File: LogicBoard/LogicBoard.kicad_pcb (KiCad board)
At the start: 2 copper layers, 96.5 x 43.9 mm, 19 parts, among them J1 Conn_01x50, J2 Conn_01x10, J3 Conn_interconn, J4 Conn_02x5_CODEC, U1 STM32H757XIHx

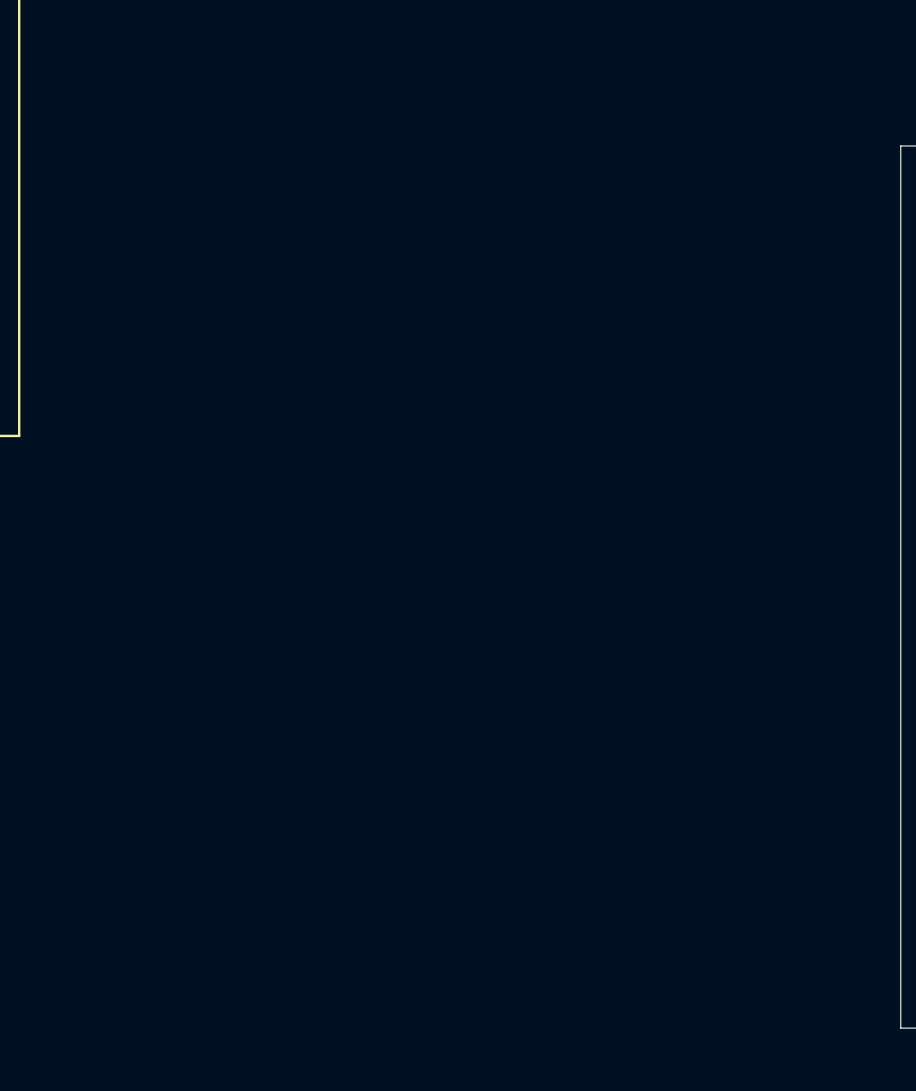
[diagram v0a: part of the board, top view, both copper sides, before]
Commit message: added jlcpcb nums to some parts
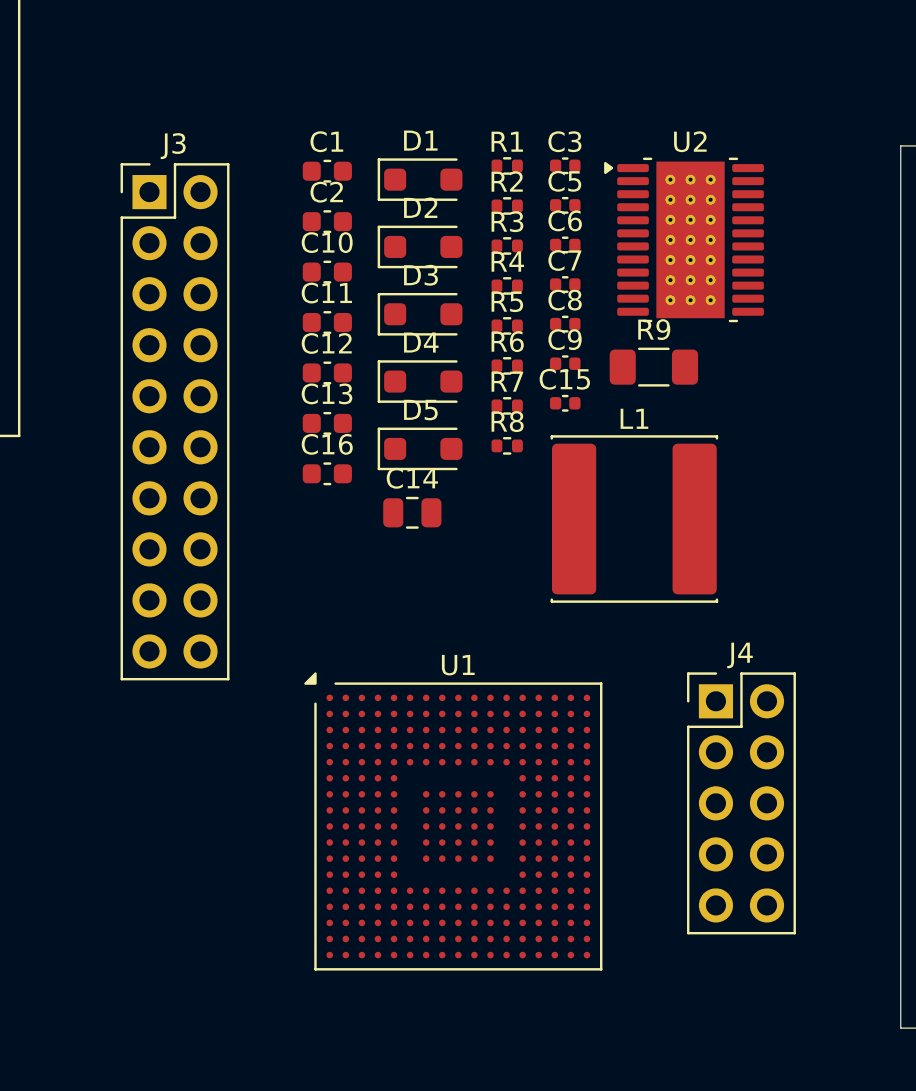
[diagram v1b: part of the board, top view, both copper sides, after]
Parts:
- added C1: 330n, Capacitor_SMD:C_0603_1608Metric, F.Cu at (76.1, 44.8)
- added C10: 1u, Capacitor_SMD:C_0603_1608Metric, F.Cu at (76.1, 49.8)
- added C11: 330n, Capacitor_SMD:C_0603_1608Metric, F.Cu at (76.1, 52.3)
- added C12: 330n, Capacitor_SMD:C_0603_1608Metric, F.Cu at (76.1, 54.8)
- added C13: 1u, Capacitor_SMD:C_0603_1608Metric, F.Cu at (76.1, 57.3)
- added C14: 22u, Capacitor_SMD:C_0805_2012Metric, F.Cu at (80.4, 61.8)
- added C15: 22p, Capacitor_SMD:C_0402_1005Metric, F.Cu at (88.0, 56.3)
- added C16: 100n, Capacitor_SMD:C_0603_1608Metric, F.Cu at (76.1, 59.8)
- added C2: 330n, Capacitor_SMD:C_0603_1608Metric, F.Cu at (76.1, 47.3)
- added C3: 220n, Capacitor_SMD:C_0402_1005Metric, F.Cu at (88.0, 44.5)
- added C5: 10n, Capacitor_SMD:C_0402_1005Metric, F.Cu at (88.0, 46.5)
- added C6: 10n, Capacitor_SMD:C_0402_1005Metric, F.Cu at (88.0, 48.4)
- added C7: 22p, Capacitor_SMD:C_0402_1005Metric, F.Cu at (88.0, 50.4)
- added C8: 2n2, Capacitor_SMD:C_0402_1005Metric, F.Cu at (88.0, 52.4)
- added C9: 2n2, Capacitor_SMD:C_0402_1005Metric, F.Cu at (88.0, 54.3)
- added D1: 1N5818, Diode_SMD:D_SOD-123F, F.Cu at (80.9, 45.2)
- added D2: 1N5818, Diode_SMD:D_SOD-123F, F.Cu at (80.9, 48.5)
- added D3: 1N5818, Diode_SMD:D_SOD-123F, F.Cu at (80.9, 51.9)
- added D4: 1N5818, Diode_SMD:D_SOD-123F, F.Cu at (80.9, 55.2)
- added D5: 1N5818, Diode_SMD:D_SOD-123F, F.Cu at (80.9, 58.6)
- added J3: Conn_interconn, Connector_PinHeader_2.54mm:PinHeader_2x10_P2.54mm_Vertical, F.Cu at (67.3, 45.8)
- added J4: Conn_02x5_CODEC, Connector_PinHeader_2.54mm:PinHeader_2x05_P2.54mm_Vertical, F.Cu at (95.5, 71.1)
- added L1: 3.9u, Inductor_SMD:L_Changjiang_FNR8040S, F.Cu at (91.4, 62.1)
- added R1: 510k, Resistor_SMD:R_0402_1005Metric, F.Cu at (85.1, 44.5)
- added R2: 100k, Resistor_SMD:R_0402_1005Metric, F.Cu at (85.1, 46.5)
- added R3: 510k, Resistor_SMD:R_0402_1005Metric, F.Cu at (85.1, 48.5)
- added R4: 510k, Resistor_SMD:R_0402_1005Metric, F.Cu at (85.1, 50.5)
- added R5: 1Meg, Resistor_SMD:R_0402_1005Metric, F.Cu at (85.1, 52.5)
- added R6: 75k, Resistor_SMD:R_0402_1005Metric, F.Cu at (85.1, 54.4)
- added R7: 68k, Resistor_SMD:R_0402_1005Metric, F.Cu at (85.1, 56.4)
- added R8: 510k, Resistor_SMD:R_0402_1005Metric, F.Cu at (85.1, 58.4)
- added R9: 0R, Resistor_SMD:R_1206_3216Metric_Pad1.30x1.75mm_HandSolder, F.Cu at (92.4, 54.5)
- added U1: STM32H757XIHx, Package_BGA:TFBGA-265_14x14mm_Layout17x17_P0.8mm, F.Cu at (82.7, 77.4)
- added U2: TPS65150PWPR, Package_SO:HTSSOP-24-1EP_4.4x7.8mm_P0.65mm_EP3.4x7.8mm_Mask2.44x3.42mm_ThermalVias, F.Cu at (94.2, 48.2)
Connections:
- J1 pad 1: /CONN_rgb_display/Bus_Disp_pwr.LED_A -> /Bus_Disp_pwr.AVDD
- J1 pad 2: /CONN_rgb_display/Bus_Disp_pwr.LED_A -> /Bus_Disp_pwr.AVDD
- J1 pad 43: /CONN_rgb_display/Bus_Disp_pwr.AVDD -> /Bus_Disp_pwr.AVDD
- J2 pad 7: /CONN_rgb_display/Bus_Disp_pwr.VCOM -> /CONN_touch_intf/+3V3
- J2 pad 8: /CONN_rgb_display/Bus_Disp_pwr.VCOM -> /CONN_touch_intf/+3V3

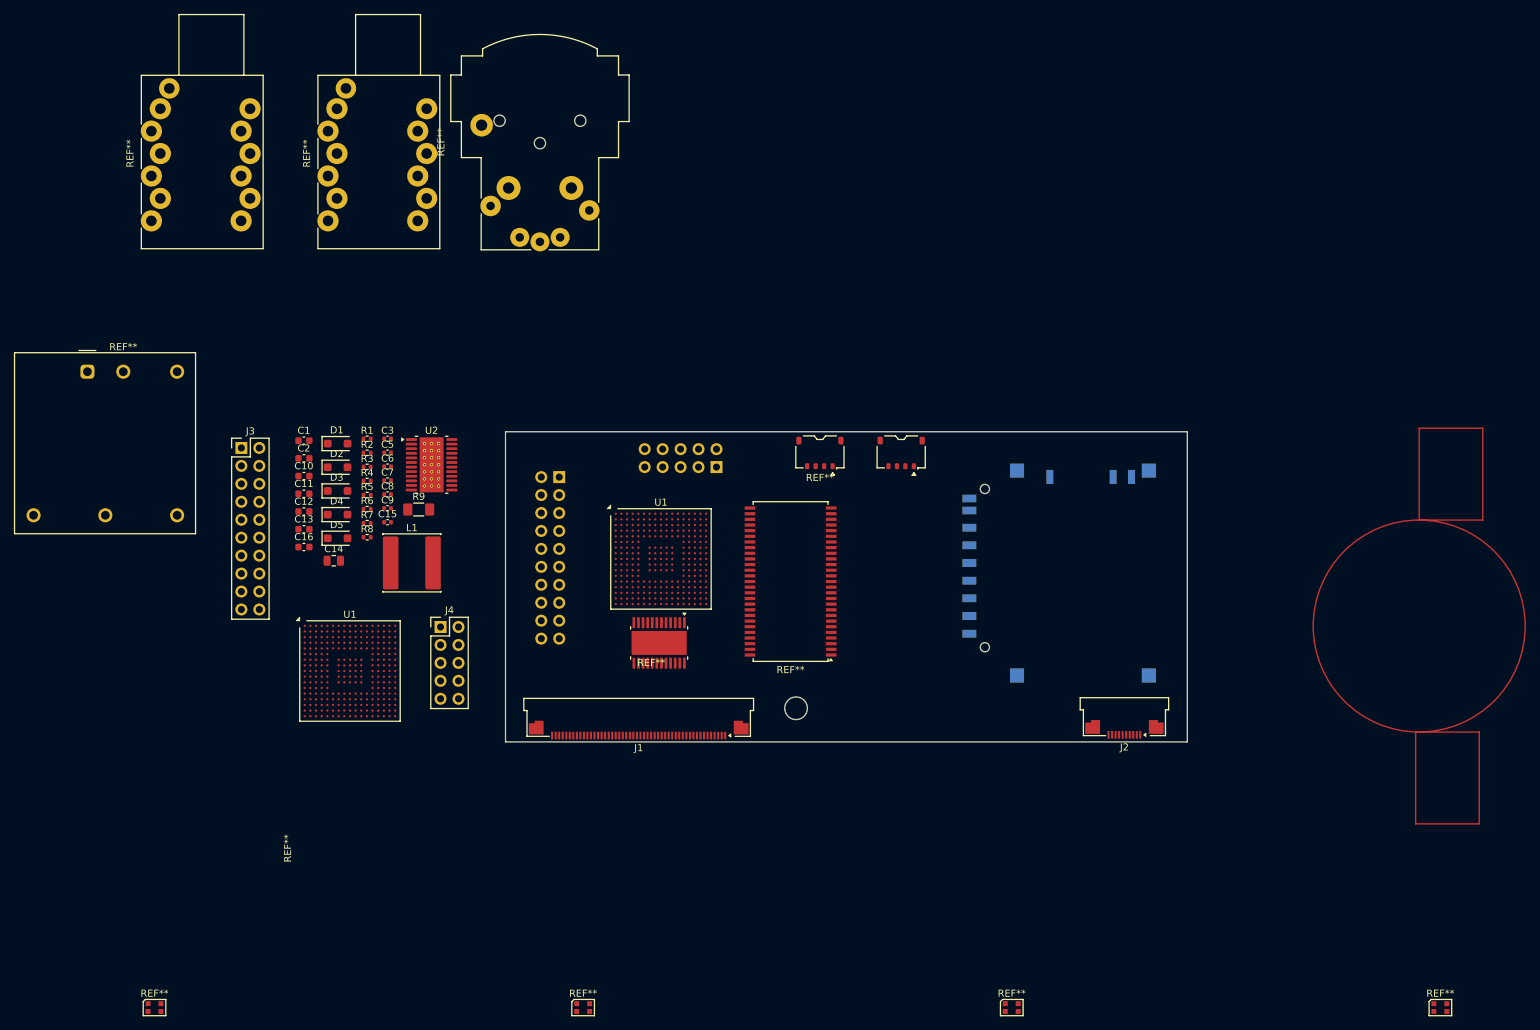
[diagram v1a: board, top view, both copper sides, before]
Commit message: Created display psu layout
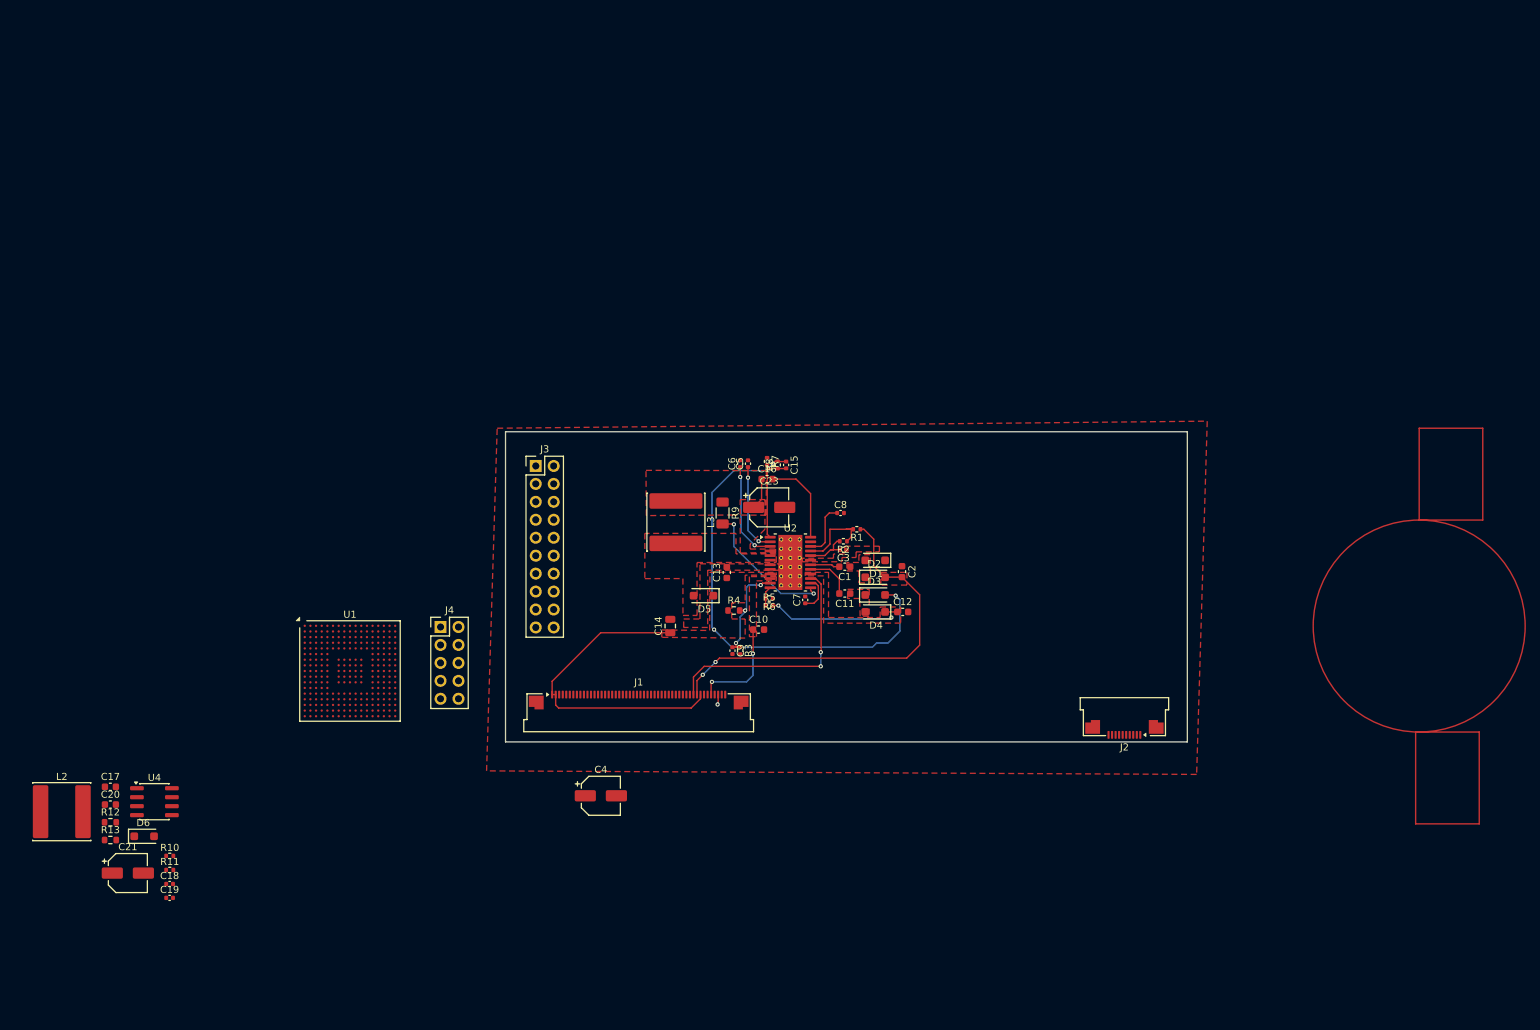
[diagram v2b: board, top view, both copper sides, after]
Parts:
- removed the J3 at (112.3, 49.9)
- removed the J4 at (134.5, 48.5)
- removed L1: 3.9u, Inductor_SMD:L_Changjiang_FNR8040S
- removed REF** (x4): LED_WS2812B-2020_PLCC4_2.0x2.0mm, LED_SMD:LED_WS2812B-2020_PLCC4_2.0x2.0mm
- removed REF**: HTSSOP-24-1EP_4.4x7.8mm_P0.65mm_EP3.4x7.8mm_Mask2.44x3.42mm, Package_SO:HTSSOP-24-1EP_4.4x7.8mm_P0.65mm_EP3.4x7.8mm_Mask2.44x3.42mm
- removed REF**: TSOP-II-54_22.2x10.16mm_P0.8mm, Package_SO:TSOP-II-54_22.2x10.16mm_P0.8mm
- removed REF**: SD_Hirose_DM1AA_SF_PEJ82, Connector_Card:SD_Hirose_DM1AA_SF_PEJ82
- removed REF**: Converter_DCDC_TRACO_THN30-xxxx_THT, Converter_DCDC:Converter_DCDC_TRACO_THN30-xxxx_THT
- removed REF** (x2): Jack_6.35mm_Neutrik_NSJ12HH-1_Horizontal, Connector_Audio:Jack_6.35mm_Neutrik_NSJ12HH-1_Horizontal
- removed REF**: MountingHole_3.2mm_M3, MountingHole:MountingHole_3.2mm_M3
- removed REF**: Jack_XLR-6.35mm_Neutrik_NCJ6FA-H_Horizontal, Connector_Audio:Jack_XLR-6.35mm_Neutrik_NCJ6FA-H_Horizontal
- removed REF** (x2): JST_ACH_BM04B-ACHSS-A-GAN-ETF_1x04-1MP_P1.20mm_Vertical, Connector_JST:JST_ACH_BM04B-ACHSS-A-GAN-ETF_1x04-1MP_P1.20mm_Vertical
- removed the U1 at (126.7, 61.5)
- added C17: 100n, Capacitor_SMD:C_0603_1608Metric, F.Cu at (48.8, 93.8)
- added C18: 10p, Capacitor_SMD:C_0402_1005Metric, F.Cu at (57.1, 107.5)
- added C19: 1n, Capacitor_SMD:C_0402_1005Metric, F.Cu at (57.1, 109.5)
- added C20: 8.2n, Capacitor_SMD:C_0603_1608Metric, F.Cu at (48.8, 96.3)
- added C21: 47u, Capacitor_SMD:CP_Elec_5x5.3, F.Cu at (51.2, 106.0)
- added C23: 22u, Capacitor_SMD:CP_Elec_5x5.4, F.Cu at (142.0, 54.2)
- added C4: 22u, Capacitor_SMD:CP_Elec_5x5.4, F.Cu at (118.2, 95.0)
- added D6: 1N5818, Diode_SMD:D_SOD-123F, F.Cu at (53.5, 100.8)
- added L2: 3.3u, Inductor_SMD:L_Changjiang_FNR8065S, F.Cu at (41.9, 97.3)
- added L3: 3.3u, Inductor_SMD:L_Changjiang_FNR8065S, F.Cu at (128.8, 56.3)
- added R10: 3.3k, Resistor_SMD:R_0402_1005Metric, F.Cu at (57.2, 103.5)
- added R11: 10k, Resistor_SMD:R_0402_1005Metric, F.Cu at (57.2, 105.5)
- added R12: 43k, Resistor_SMD:R_0603_1608Metric, F.Cu at (48.8, 98.8)
- added R13: 390R, Resistor_SMD:R_0603_1608Metric, F.Cu at (48.8, 101.3)
- added U4: TPS54331DR, Package_SO:SOIC-8_3.9x4.9mm_P1.27mm, F.Cu at (55.0, 95.9)
- R3: value 510k -> 330k
- R4: value 510k -> 680k; footprint Resistor_SMD:R_0402_1005Metric -> Resistor_SMD:R_0603_1608Metric
- U2: footprint Package_SO:HTSSOP-24-1EP_4.4x7.8mm_P0.65mm_EP3.4x7.8mm_Mask2.44x3.42mm_ThermalVias -> Package_SO:HTSSOP-24-1EP_4.4x7.8mm_P0.65mm_EP3.4x7.8mm_Mask2.4x4.68mm_ThermalVias
- moved C2 86.2 mm to (160.8, 63.3), turned to -90 degrees
- moved C12 85.9 mm to (160.9, 69.0)
- moved C1 78.6 mm to (152.7, 62.6), turned to 180 degrees
- moved D1 77.9 mm to (157.0, 61.7), turned to 180 degrees
- moved C11 77.8 mm to (152.7, 66.4), turned to 180 degrees
- moved D2 77.7 mm to (157.0, 64.1)
- moved D3 77.5 mm to (157.0, 66.6)
- moved D4 77.3 mm to (157.0, 69.0), turned to 180 degrees
- moved R1 70.5 mm to (154.4, 57.3), turned to 180 degrees
- moved R2 68.6 mm to (152.5, 59.0), turned to 180 degrees
- moved C10 67.9 mm to (140.5, 71.5)
- moved C3 66.4 mm to (152.5, 60.2), turned to 180 degrees
- moved C16 66.3 mm to (141.7, 50.2)
- moved C8 64.2 mm to (152.1, 55.0)
- moved C7 61.5 mm to (147.1, 67.3), turned to 90 degrees
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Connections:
- net Net-(D4-K) renamed /PowerSection/CPI
- net Net-(D5-A) renamed /PowerSection/SW
- net Net-(U2-ADJ) renamed /PowerSection/ADJ
- net Net-(U2-COMP) renamed /PowerSection/COMP
- net Net-(U2-CTRL) renamed /PowerSection/CTRL
- net Net-(U2-DLY1) renamed /PowerSection/DLY1
- net Net-(U2-DLY2) renamed /PowerSection/DLY2
- net Net-(U2-DRVN) renamed /PowerSection/DRVN
- net Net-(U2-DRVP) renamed /PowerSection/DRVP
- net Net-(U2-FB) renamed /PowerSection/FB
- net Net-(U2-FBN) renamed /PowerSection/FBN
- net Net-(U2-FBP) renamed /PowerSection/FBP
- net Net-(U2-IN) renamed /PowerSection/IN
- net Net-(U2-REF) renamed /PowerSection/REF
- C11 pad 1: Net-(D3-K) -> Net-(D3-A)
- D3 pad 1: Net-(D3-K) -> /Bus_Disp_pwr.AVDD
- D3 pad 2: unconnected-(D3-A-Pad2) -> Net-(D3-A)
- D4 pad 2: Net-(D3-K) -> Net-(D3-A)
- J1 pad 3: /CONN_rgb_display/Bus_Disp_pwr.LED_K -> GND
- J1 pad 4: /CONN_rgb_display/Bus_Disp_pwr.LED_K -> GND
- U2 pad 25: (no net) -> GND
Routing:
- net /Bus_Disp_pwr.AVDD: track 0.00 -> 113.6 mm, vias 0 -> 3
- net /CONN_rgb_display/Bus_Disp_pwr.VGL: track 0.00 -> 57.3 mm, vias 0 -> 2
- net /CONN_rgb_display/Bus_Disp_pwr.VGH: track 0.00 -> 34.6 mm, vias 0 -> 2
- net /PowerSection/CTRL: track 0.00 -> 19.8 mm, vias 0 -> 2
- net /PowerSection/CPI: track 0.00 -> 19.4 mm, vias 0 -> 2
- net /PowerSection/IN: track 0.00 -> 15.1 mm, vias 0 -> 3
- net /CONN_rgb_display/Bus_Disp_pwr.VCOM: track 0.00 -> 14.5 mm, vias 0 -> 2
- net /PowerSection/DLY2: track 0.00 -> 14.2 mm, vias 0 -> 2
- net /PowerSection/FB: track 0.00 -> 13.1 mm
- net /PowerSection/DLY1: track 0.00 -> 12.8 mm, vias 0 -> 2
- net Net-(U2-FDLY): track 0.00 -> 12.4 mm
- net /PowerSection/FBN: track 0.00 -> 11.2 mm
- net /PowerSection/COMP: track 0.00 -> 7.82 mm
- net /PowerSection/REF: track 0.00 -> 6.71 mm
- net /PowerSection/DRVP: track 0.00 -> 6.70 mm
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- added copper zone on F.Cu, net /Bus_Disp_pwr.AVDD
- added copper zone on F.Cu, net /CONN_rgb_display/Bus_Disp_pwr.VCOM
- added copper zone on F.Cu, net /CONN_rgb_display/Bus_Disp_pwr.VGL
- added copper zone on F.Cu, net /PowerSection/5V
- added copper zone on F.Cu, net /PowerSection/CPI
- added copper zone on F.Cu, net /PowerSection/SW
- added copper zone on F.Cu, net GND
- added copper zone on F.Cu, net Net-(D1-A)
- added copper zone on F.Cu, net Net-(D3-A)
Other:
- copper layers 2 -> 4

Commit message: experimenting with bga
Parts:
- added C22: 12p, Capacitor_SMD:C_0402_1005Metric, F.Cu at (147.9, 58.0)
- added C24: 12p, Capacitor_SMD:C_0402_1005Metric, F.Cu at (150.9, 61.5)
- added REF**: BGA-90_8.0x13.0mm_Layout2x3x15_P0.8mm, Package_BGA:BGA-90_8.0x13.0mm_Layout2x3x15_P0.8mm, F.Cu at (173.5, 61.5)
- added REF**: Alliance_TFBGA-54_8x8mm_Layout9x9_P0.8mm, Package_BGA:Alliance_TFBGA-54_8x8mm_Layout9x9_P0.8mm, F.Cu at (152.5, 79.0)
- added REF**: TSOP-II-54_22.2x10.16mm_P0.8mm, Package_SO:TSOP-II-54_22.2x10.16mm_P0.8mm, F.Cu at (158.7, 79.2)
- added Y1: X322525MOB4SI 25MHZ, Crystal:Crystal_SMD_3225-4Pin_3.2x2.5mm, F.Cu at (148.4, 60.8)
- D1, D2, D3, D4, D5, D6: value 1N5818 -> MBRS130LT3G; footprint Diode_SMD:D_SOD-123F -> Diode_SMD:D_SMB
- J3: moved to B.Cu
- moved C17 153.2 mm to (191.1, 37.0)
- moved C18 153.2 mm to (199.5, 50.8)
- moved C19 153.2 mm to (199.5, 52.8)
- moved C20 153.2 mm to (191.1, 39.5)
- moved C21 153.2 mm to (193.6, 49.2)
- moved R12 153.2 mm to (191.1, 42.1)
- moved R13 153.2 mm to (191.1, 44.6)
- moved D6 153.2 mm to (195.9, 44.0)
- moved L2 153.2 mm to (184.2, 40.6)
- moved R10 153.2 mm to (199.5, 46.8)
- moved R11 153.2 mm to (199.5, 48.8)
- moved U4 153.2 mm to (197.3, 39.1)
- moved C4 81.3 mm to (185.1, 48.8)
- moved U1 79.0 mm to (160.0, 61.1)
- moved J4 77.1 mm to (166.2, 40.5), turned to 90 degrees
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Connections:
- U1 pad J1: unconnected-(U1-PH1-PadJ1) -> /mcu/OSC_OUT
- U1 pad J2: unconnected-(U1-PH0-PadJ2) -> /mcu/OSC_IN
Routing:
- net /CONN_rgb_display/Bus_Disp_pwr.VGL: track 57.3 -> 14.9 mm
- net /Bus_Disp_pwr.AVDD: track 113.6 -> 142.8 mm, vias 3 -> 7
- net /PowerSection/CPI: track 19.4 -> 9.84 mm
- net /mcu/OSC_IN: track 0.00 -> 9.47 mm, vias 0 -> 2
- net /mcu/OSC_OUT: track 0.00 -> 4.75 mm, vias 0 -> 1
- net /PowerSection/FBN: track 11.2 -> 8.03 mm
- net /PowerSection/DRVN: track 4.18 -> 6.79 mm
- net /PowerSection/REF: track 6.71 -> 5.86 mm
- net /PowerSection/COMP: track 7.82 -> 7.03 mm
- added copper zone on F.Cu, net /PowerSection/DRVN
- added copper zone on F.Cu, net /PowerSection/DRVP
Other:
- board size 96.5 x 43.9 mm -> 100 x 55 mm
